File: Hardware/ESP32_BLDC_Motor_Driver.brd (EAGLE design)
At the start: 85.1 x 61 mm, 184 parts, among them J1 USB-C Connector, J4 Breadboard Connector, J5 Breadboard Headers, J7 QWIIC_RIGHT_ANGLE, P1 0532610371, Q2 NPN Transistors, Q3 20V/4.2A/52mΩ/1.4W, U1 TMC6300, U2 3.3V, U3 ESP-WROOM-3232D, U4 CH340C, U5 ESD Diode, U6 AP63357, U8 TMAG5273, U9 LMV324

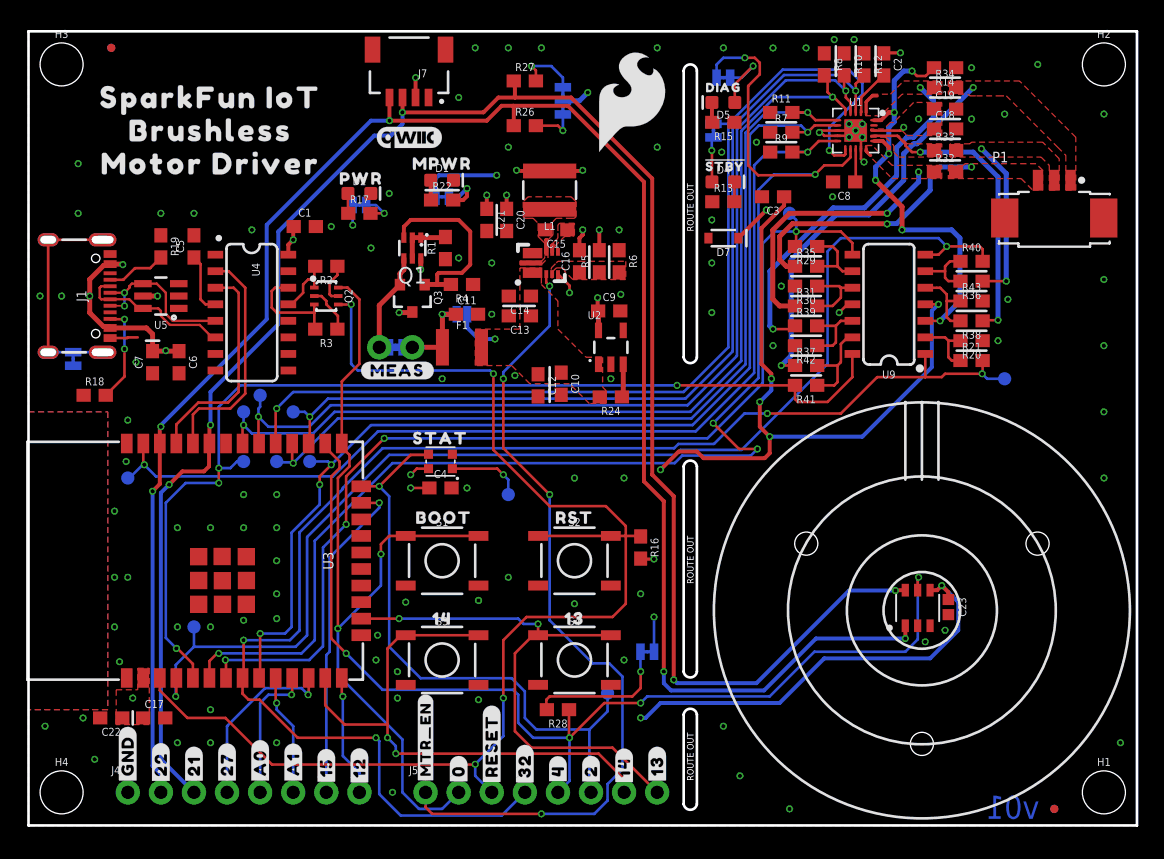
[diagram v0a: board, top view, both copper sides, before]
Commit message: V10 INITIAL COMMIT
Added datasheets for new parts; created new library component for the INA240 inline current sensing; lined up other parts for symmetry; redid the OPA344 current sensing section
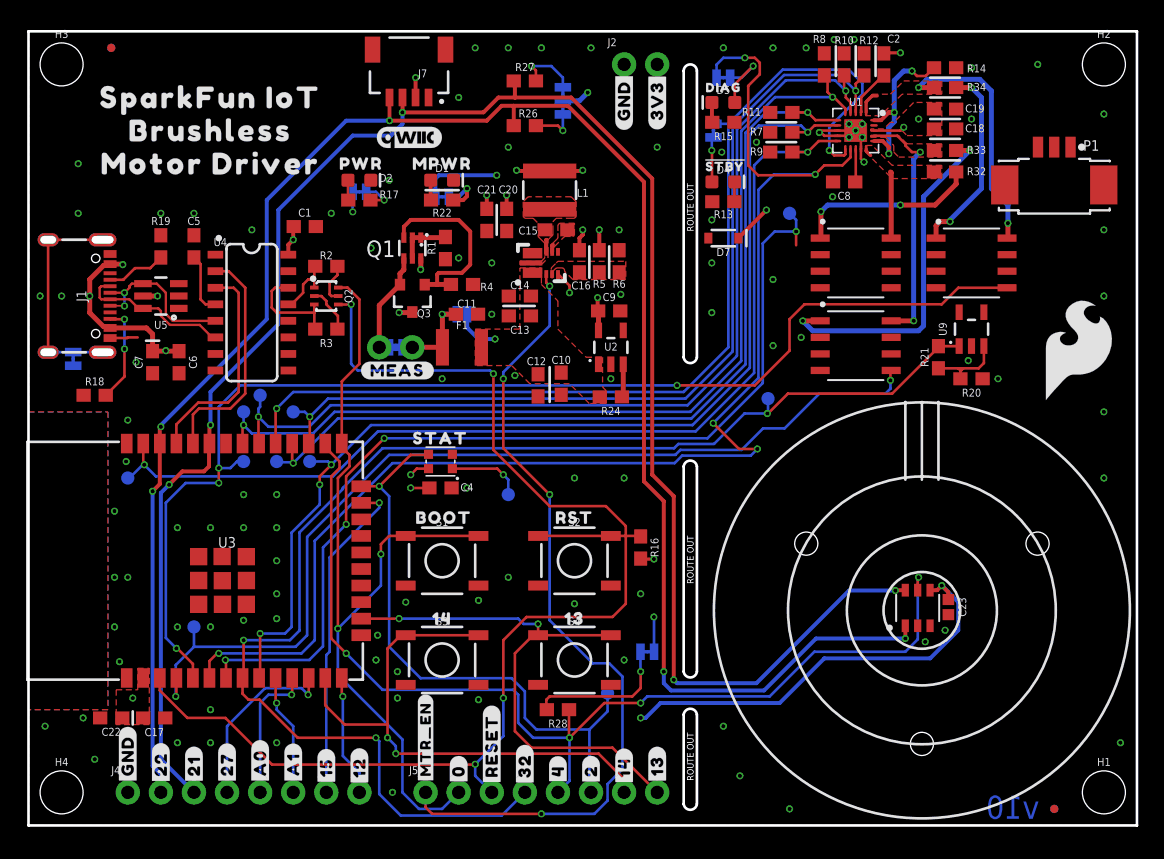
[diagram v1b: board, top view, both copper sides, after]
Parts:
- removed C3: 0.1uF, SparkFun-Capacitors:0603
- removed R29, R30, R40, R41, R42, R43: 20k, SparkFun-Resistors:0603
- removed R31, R35, R36, R37, R38, R39: 1k, SparkFun-Resistors:0603
- added J2: (no value), SparkFun-Connectors:1X02_NO_SILK
- added U$28: (no value), output:#GND#17
- added U$58: (no value), output:#3V3#18
- added U10, U11, U7: INA240A1, INA240A1:D8_TEX
- U9: value LMV324 -> OPA344; device SparkFun-IC-Amplifiers:SO14 -> SparkFun-IC-Amplifiers:SOT23-5
- moved LOGO3 39.2 mm to (80.6, 36.4)
- moved TP9 18.2 mm to (56.8, 32.8)
- moved U9 6.48 mm to (72.4, 38.1), turned to 0 degrees
- moved R20 2.92 mm to (72.4, 34.3)
- moved R21 2.55 mm to (69.8, 35.9), turned to 90 degrees
- moved P1 2.54 mm to (78.7, 52.1)
- moved U$12 1.14 mm to (25.5, 50.8)
- moved D2 1.02 mm to (25.4, 49.5)
- moved PWR 1.02 mm to (25.4, 48.6)
- moved R17 1.02 mm to (25.4, 48.0)
- moved U$27 1.02 mm to (25.4, 50.4)
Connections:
- removed net N$16: R29.1, R35.2, U9.9
- removed net N$18: R30.1, R31.2, U9.10
- removed net N$19: R36.2, R40.1, U9.6
- removed net N$20: R38.2, R43.1, U9.5
- removed net N$24: R37.2, R41.1, U9.13
- removed net N$25: R39.2, R42.1, U9.12
- new net N$10: U9.4
- net 3.3V: now also J2.2, U10.3, U10.6, U11.3, U11.6, U7.3, U7.6, U9.5; no longer C3.1, U9.4
- net ESP_35/U_OUT: now also U7.5; no longer R29.2, U9.8
- net ESP_36/V_OUT: now also U11.5; no longer R40.2, U9.7
- net ESP_39/W_OUT: now also U10.5; no longer R41.2, U9.14
- net GND: now also J2.1, U10.2, U10.7, U11.2, U11.7, U7.2, U7.7, U9.2; no longer C3.2, R30.2, R42.2, R43.2, U9.11
- net N$14: now also U9.3; no longer U9.2
- net SENSE: no longer U9.3
- net SENSE_U: now also U7.8; no longer R31.1
- net SENSE_V: now also U11.8; no longer R38.1
- net SENSE_W: now also U10.8; no longer R39.1
- net U: now also U7.1; no longer R35.1
- net V: now also U11.1; no longer R36.1
- net W: now also U10.1; no longer R37.1
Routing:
- net 3.3V: track 101.7 -> 50.3 mm, vias 18 -> 13
- net SENSE: track 33.1 -> 13.2 mm, vias 6 -> 3
- net ESP_36/V_OUT: track 93.6 -> 74.9 mm
- net SENSE_U: track 21.4 -> 5.75 mm, vias 2 -> 0
- net W: track 30.1 -> 14.9 mm
- net V: track 12.8 -> 27.1 mm
- net ESP_39/W_OUT: track 80.0 -> 92.7 mm
- net SENSE_W: track 29.6 -> 21.1 mm
- net N$24: track 7.35 -> 0.00 mm
- net U: track 20.8 -> 14.2 mm
- net N$20: track 5.83 -> 0.00 mm
- net N$16: track 5.72 -> 0.00 mm, vias 0 -> 1
- net ESP_35/U_OUT: track 80.1 -> 74.4 mm
- net N$25: track 5.67 -> 0.00 mm
- net N$18: track 5.59 -> 0.00 mm
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- removed copper zone on layer 1, net U
- removed copper zone on layer 1, net V
- removed copper zone on layer 1, net W
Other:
- board text added: "v10"
- board text removed: "v01"

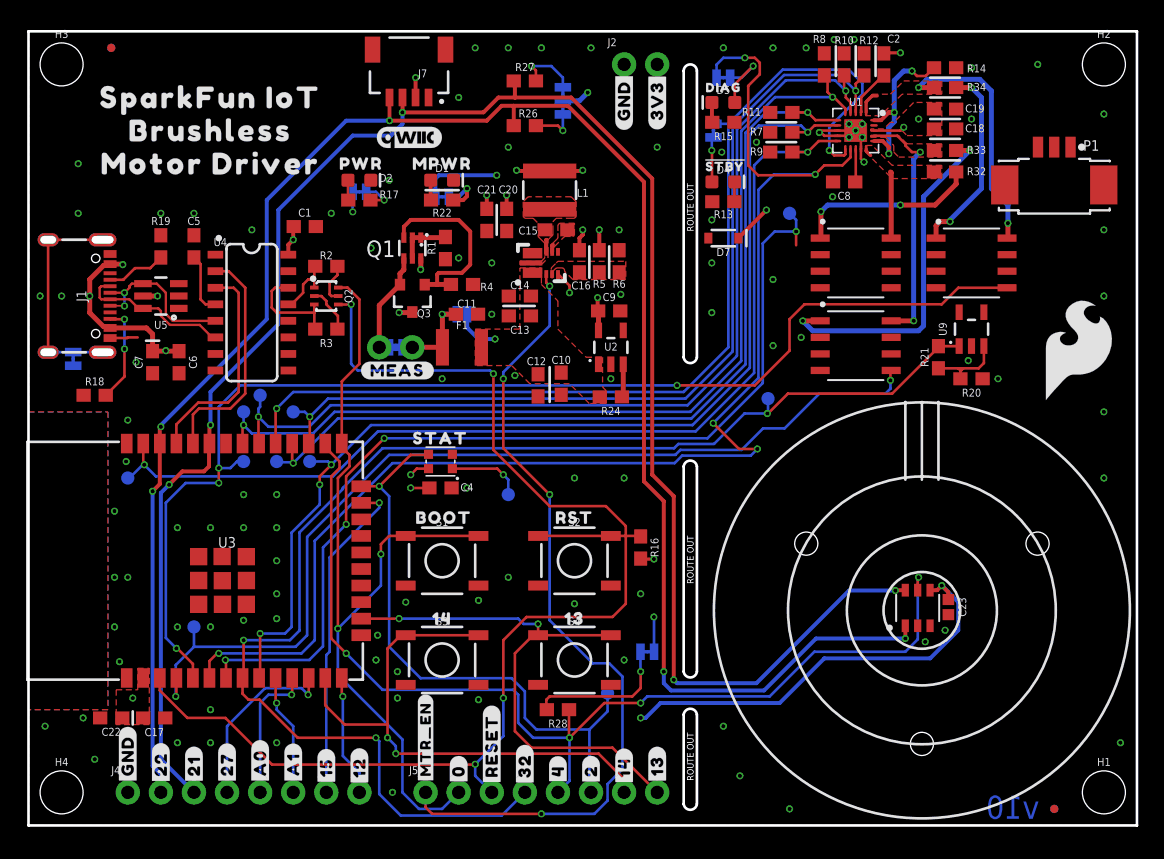
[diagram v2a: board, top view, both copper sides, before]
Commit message: Reds Review - final changes
Deleted datasheets no longer needed; updated documents to parts currently on board; added more GND vias to GND return paths on the layout; Fixed the OPA344 op amp section; added decoupling caps to the current sense op amp and the inline current sense op amps; turned the motor and updated the silk to be correct; adjusted the output connector to the motor to be further away leaving less extra wire; panelized board files for production/ordering review; changed the part INA240A1 to have pinout consistent with other components in the SparkFun library; Added more test points for the output to the motor;
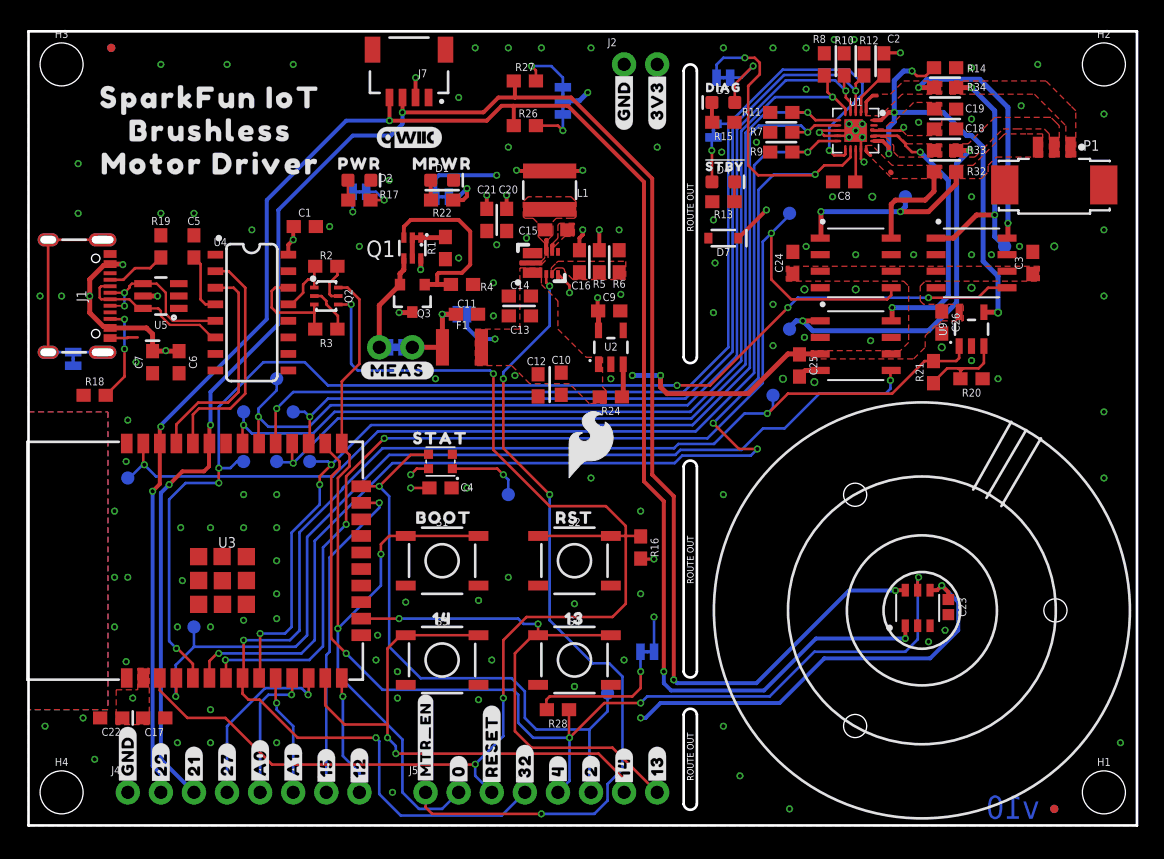
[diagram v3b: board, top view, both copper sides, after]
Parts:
- added C24, C25, C26, C3: 0.1uF, SparkFun-Capacitors:0603
- added LOGO1: SFE_LOGO_NAMEBLANK, SparkFun-Aesthetics:BLANK
- added TP13, TP14, TP15: TEST-POINT3X4, SparkFun-Connectors:PAD.03X.04
- LOGO3: value SFE_LOGO_FLAME.3_INCH -> SFE_LOGO_FLAME.2_INCH; device SparkFun-Aesthetics:SFE_LOGO_FLAME_.3 -> SparkFun-Aesthetics:SFE_LOGO_FLAME_.2
- moved LOGO3 38.2 mm to (43.2, 29.2)
- moved U$62 2.54 mm to (68.6, 27.9)
- moved U$55 2.54 mm to (68.6, 30.5)
- moved TP5 1.80 mm to (19.1, 34.3)
- moved R21 1.20 mm to (69.5, 34.8)
- moved TP9 0.46 mm to (57.1, 33.0)
- moved U$12 0.13 mm to (25.4, 50.8)
- turned U$2 to 330 degrees
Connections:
- removed net N$10: U9.4
- net 3.3V: now also C24.1, C25.1, C26.1, C3.1
- net GND: now also C24.2, C25.2, C26.2, C3.2, U10.4, U11.4, U7.4
- net SENSE: now also U9.4
- net U: now also TP13.1
- net V: now also TP14.1
- net W: now also TP15.1
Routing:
- net SENSE: track 13.2 -> 35.4 mm, vias 3 -> 4
- net 3.3V: track 50.3 -> 67.1 mm, vias 13 -> 14
- net ESP_35/U_OUT: track 74.4 -> 86.0 mm
- net W: track 14.9 -> 19.7 mm
- net SENSE_V: track 19.0 -> 21.8 mm
- net SENSE_U: track 5.75 -> 8.51 mm
- net V: track 27.1 -> 28.9 mm
- net GND: track 13.0 -> 14.8 mm, vias 102 -> 131
- net ESP_18/VH: track 73.7 -> 75.5 mm
- net U: track 14.2 -> 15.5 mm
- net ESP_32/CURR_SENSE: track 102.8 -> 103.7 mm
- net N$14: track 6.57 -> 7.20 mm
- net ESP_39/W_OUT: track 92.7 -> 92.6 mm, vias 4 -> 6
- added copper zone on layer 1, net U
- added copper zone on layer 1, net V
- added copper zone on layer 1, net W

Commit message: Changes from Reds Review
Fixed INA240A1 symbol; changed voltage input range; adjusted OPA344 to be non-inverting; SENSE trace now 30mil instead of 15mil; moved inline current sense resistors to allow kelvin connections; moved connector down and turned motor to allow better polygon connections for U; Reworked 3.3V power distribution with Op Amps and changed  caps to be on power pin rather than reference; changed some silk names; turned thermals off.
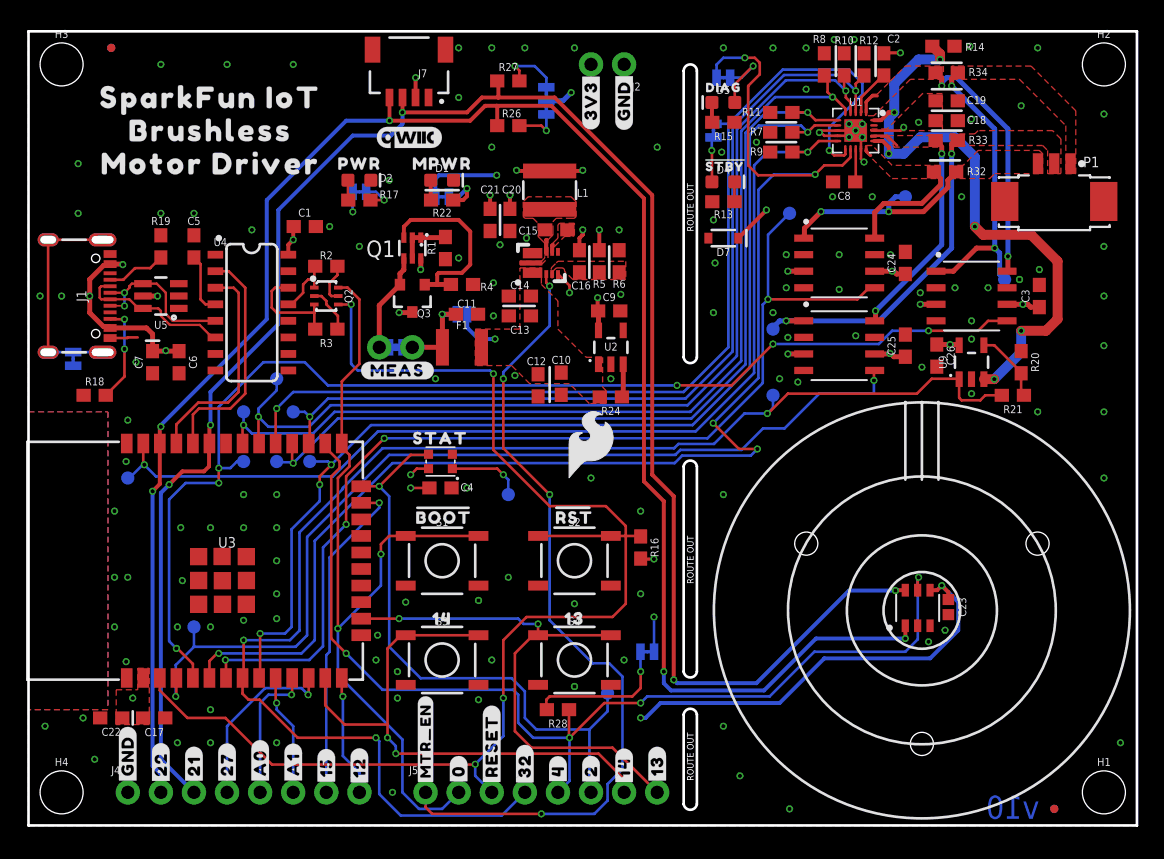
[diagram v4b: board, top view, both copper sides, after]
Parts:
- added U$59: (no value), output:#2#RGB#18
- added U$60: (no value), output:#GND#17
- U$16: device output:#2#LED#21630063003534 -> output:#3V3#18
- U$32: device output:#0#QWR#36 -> output:#0##BOOT##0
- moved U$16 49.5 mm to (43.2, 55.6)
- moved FRAME1 19.0 mm to (19.1, -83.8)
- moved C24 8.64 mm to (67.3, 43.2)
- moved C25 8.27 mm to (67.3, 36.8), turned to 90 degrees
- moved R21 6.35 mm to (75.6, 33.0), turned to 180 degrees
- moved U$58 5.08 mm to (43.2, 55.6)
- moved R20 4.02 mm to (76.2, 35.6), turned to 270 degrees
- moved C3 2.59 mm to (77.6, 40.6)
- moved C26 2.57 mm to (69.7, 36.1)
- moved TP15 2.54 mm to (74.9, 41.9)
- moved U10 2.54 mm to (72.4, 40.6)
- moved U9 2.54 mm to (72.4, 35.6)
- moved R14 1.66 mm to (70.2, 59.8)
- moved I2C 1.27 mm to (39.8, 55.6)
- moved P1 1.27 mm to (78.7, 50.8)
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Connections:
- net N$14: now also U9.4; no longer U9.3
- net SENSE: now also U9.3; no longer U9.4
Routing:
- net SENSE: track 35.4 -> 48.3 mm, vias 4 -> 6
- net ESP_35/U_OUT: track 86.0 -> 80.5 mm
- net SENSE_V: track 21.8 -> 17.6 mm
- net 3.3V: track 67.1 -> 63.1 mm, vias 14 -> 19
- net ESP_32/CURR_SENSE: track 103.7 -> 107.0 mm
- net W: track 19.7 -> 23.0 mm
- net V: track 28.9 -> 26.3 mm
- net GND: track 14.8 -> 13.0 mm, vias 131 -> 134
- net N$14: track 7.20 -> 5.58 mm
- net SENSE_U: track 8.51 -> 9.75 mm
- net U: track 15.5 -> 16.7 mm
- net ESP_39/W_OUT: track 92.6 -> 91.5 mm
- net ESP_36/V_OUT: track 74.9 -> 73.8 mm
- net ESP_22/TP_SCL: track 147.6 -> 146.8 mm
- net ESP_21/TP_SDA: track 148.3 -> 147.6 mm

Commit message: Updated files for ordering
Completed all the final requests from the re-review after the reds review; double checked the test points to the test board; updated pcb spacers; updated files for ordering boards
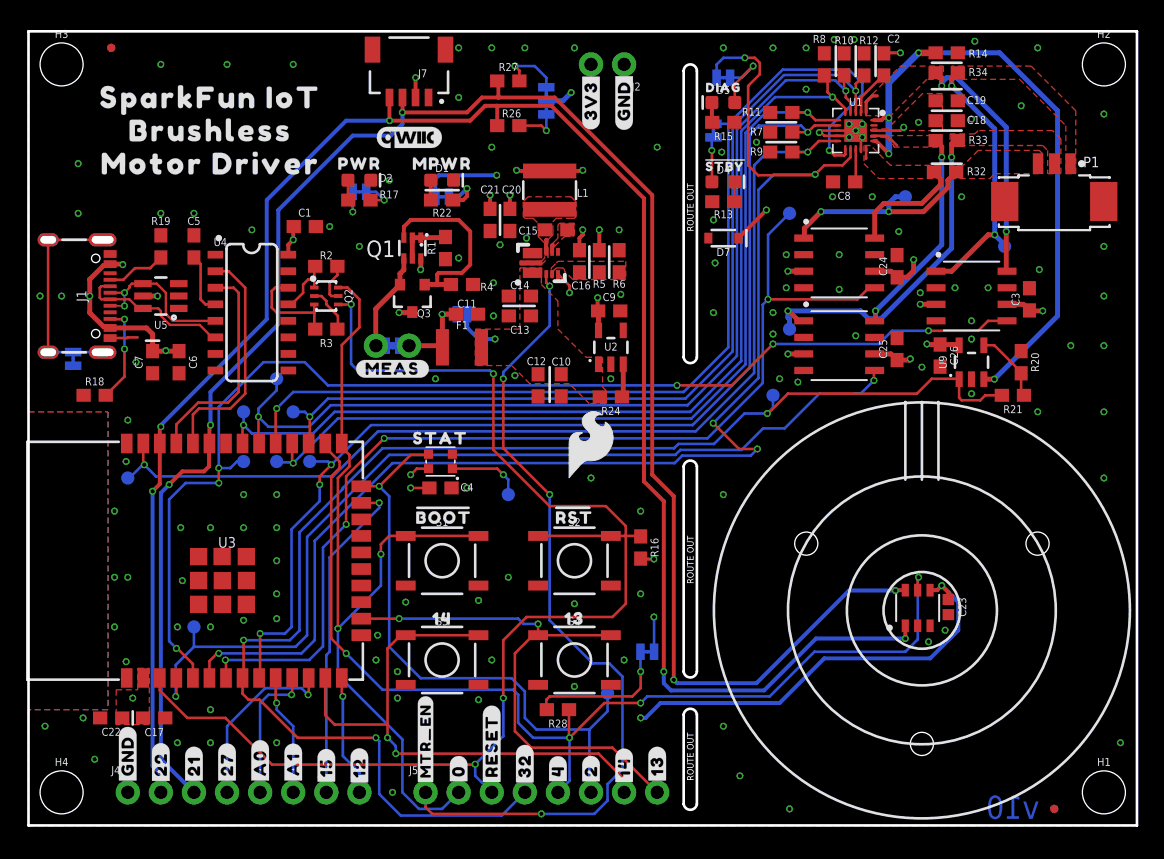
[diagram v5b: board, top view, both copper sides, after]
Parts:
- moved FRAME1 6.35 mm to (19.1, -90.2)
- moved TP15 2.54 mm to (74.9, 44.5)
- moved TP14 1.27 mm to (58.4, 38.1)
- moved C3 0.80 mm to (76.8, 40.4)
- moved C24 0.68 mm to (66.7, 42.9)
- moved C25 0.68 mm to (66.7, 36.6)
- moved R14 0.57 mm to (70.5, 59.3)
- moved U$50 0.54 mm to (27.9, 38.7)
- moved U$48 0.40 mm to (27.9, 35.1)
- moved MEAS 0.28 mm to (27.9, 36.8)
- moved C26 0.25 mm to (70.0, 36.1)
- moved C10 0.13 mm to (40.9, 33.8)
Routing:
- net 3.3V: track 63.1 -> 66.6 mm
- net W: track 23.0 -> 20.9 mm
- net GND: track 13.0 -> 12.0 mm, vias 134 -> 133
- net SENSE_V: track 17.6 -> 18.3 mm
- net ESP_36/V_OUT: track 73.8 -> 73.2 mm
- net SENSE: track 48.3 -> 48.7 mm, vias 6 -> 4
